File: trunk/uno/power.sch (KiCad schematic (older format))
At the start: 18 parts, among them Q1 FDN340P, U1 NCP1117 5V, U2 LP2985-33DBVR, U5 LM358

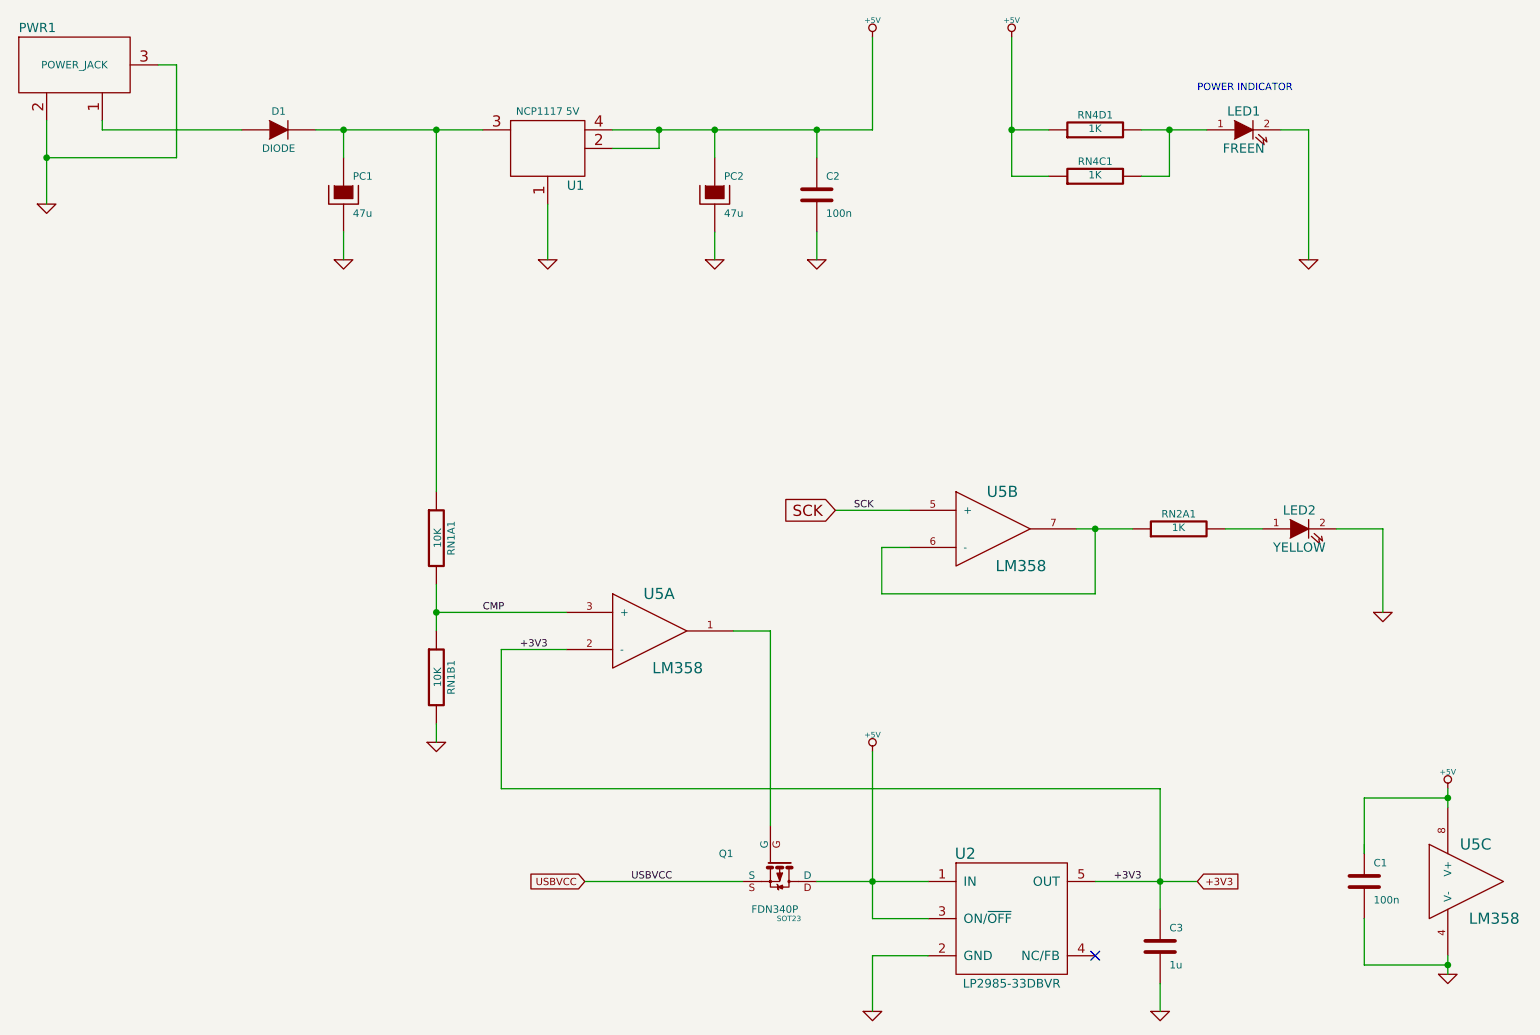
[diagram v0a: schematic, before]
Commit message: Schematic ERC passes. Circuit _might_ be complete, without errors. You just never know. :-P
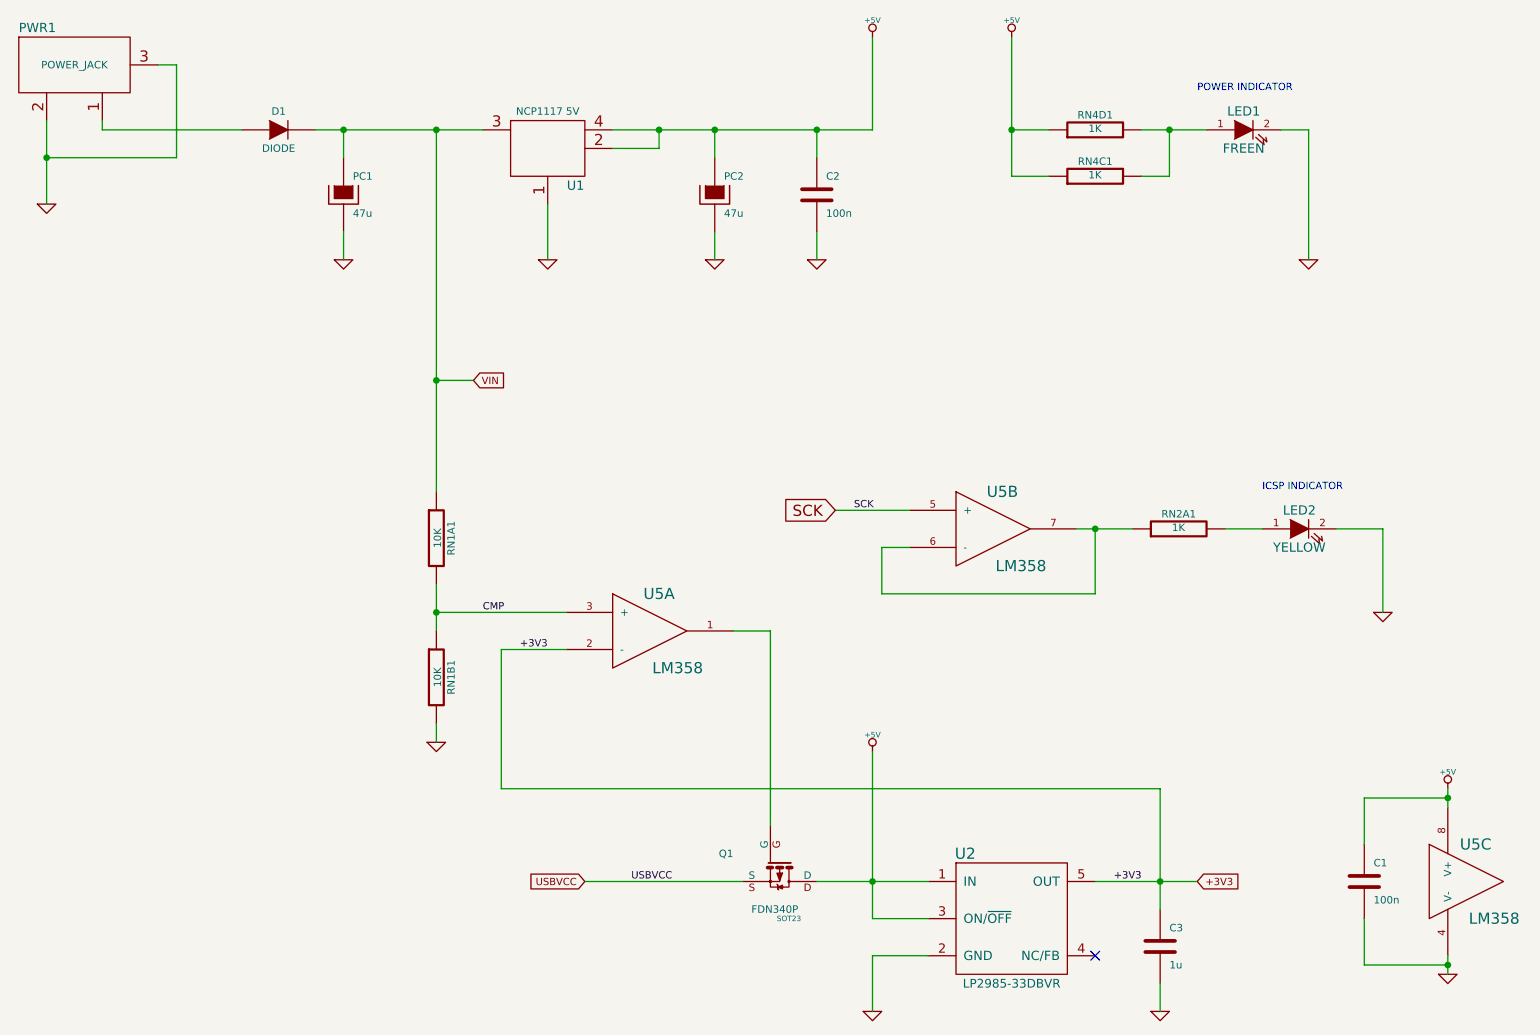
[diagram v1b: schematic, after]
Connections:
- net +5V: now also C1.1
- net VIN: now reaches D1.2 (K), PC1.1, RN1A1.1, U1.3 (IN)
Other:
- note added: "ICSP INDICATOR"
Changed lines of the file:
@@
 $EndComp
-Wire Wire Line
-	9200 5700 9200 5400
 Wire Wire Line
 	9200 5400 9650 5400
@@
 Text Notes 8300 1600 0    39   ~ 0
 POWER INDICATOR
+Text Notes 8650 3750 0    39   ~ 0
+ICSP INDICATOR
+Wire Wire Line
+	9200 5650 9200 5400
+Wire Wire Line
+	4200 3150 4400 3150
+Connection ~ 4200 3150
+Text GLabel 4400 3150 2    39   Input ~ 0
+VIN
 $EndSCHEMATC

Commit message: Component packages configured.
PCB initial placement.

Some minor typo corrections.
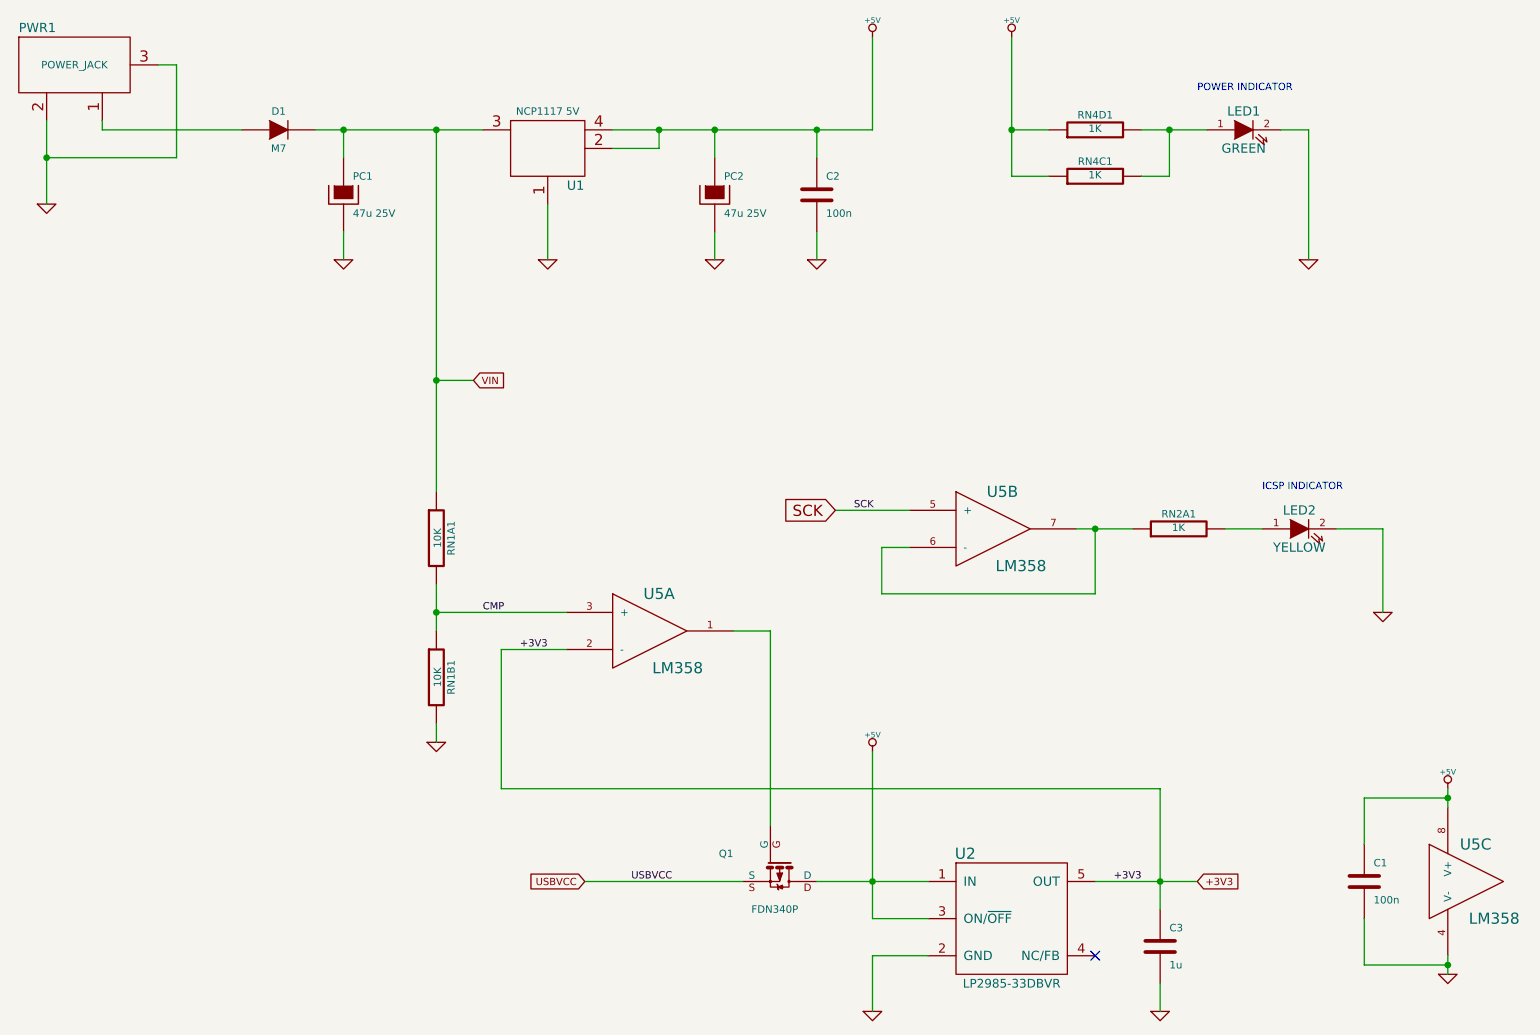
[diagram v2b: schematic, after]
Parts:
- C1, C2, C3: footprint ~ -> SM0603_Capa
- D1: value DIODE -> M7; footprint ~ -> DO-214AC
- LED1: value FREEN -> GREEN; footprint ~ -> LED_0603_GREEN
- LED2, RN1A1, RN1B1, RN2A1, RN4C1, RN4D1: footprint ~ -> (none)
- PC1, PC2: value 47u -> 47u 25V; footprint ~ -> (none)
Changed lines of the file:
@@
 Sheet 3 3
 Title "KiCADuino UNO Rev3"
-Date "24 jul 2013"
+Date "25 jul 2013"
 Rev "0.1"
 Comp "Gruvin & Co"
@@
 F 0 "U5" H 7250 4150 60  0000 C CNN
 F 1 "LM358" H 7350 3750 60  0000 C CNN
-F 2 "" H 7200 3950 60  0000 C CNN
+F 2 "" H 7200 3950 60  0001 C CNN
 F 3 "" H 7200 3950 60  0000 C CNN
 	2    7200 3950
@@
 F 0 "U5" H 5400 4700 60  0000 C CNN
 F 1 "LM358" H 5500 4300 60  0000 C CNN
-F 2 "" H 5350 4500 60  0000 C CNN
+F 2 "" H 5350 4500 60  0001 C CNN
 F 3 "" H 5350 4500 60  0000 C CNN
 	1    5350 4500
@@
 F 0 "U5" H 9800 6050 60  0000 C CNN
 F 1 "LM358" H 9900 5650 60  0000 C CNN
-F 2 "" H 9750 5850 60  0000 C CNN
+F 2 "" H 9750 5850 60  0001 C CNN
 F 3 "" H 9750 5850 60  0000 C CNN
 	3    9750 5850
@@
 F 0 "C1" H 9250 5950 40  0000 L CNN
 F 1 "100n" H 9250 5750 40  0000 L CNN
-F 2 "~" H 9238 5700 30  0000 C CNN
+F 2 "SM0603_Capa" H 9238 5700 30  0001 C CNN
 F 3 "~" H 9200 5850 60  0000 C CNN
 	1    9200 5850
@@
 F 0 "RN1A1" V 4280 4000 40  0000 C CNN
 F 1 "10K" V 4207 4001 40  0000 C CNN
-F 2 "~" V 4130 4000 30  0000 C CNN
+F 2 "" V 4130 4000 30  0001 C CNN
 F 3 "~" H 4200 4000 30  0000 C CNN
 	1    4200 4000
@@
 F 0 "RN1B1" V 4280 4750 40  0000 C CNN
 F 1 "10K" V 4207 4751 40  0000 C CNN
-F 2 "~" V 4130 4750 30  0000 C CNN
+F 2 "" V 4130 4750 30  0001 C CNN
 F 3 "~" H 4200 4750 30  0000 C CNN
 	1    4200 4750
@@
 F 0 "Q1" V 6000 5500 40  0000 R CNN
 F 1 "FDN340P" V 6300 5850 40  0000 R CNN
-F 2 "SOT23" V 6350 5800 29  0000 C CNN
+F 2 "SOT23" V 6350 5800 29  0001 C CNN
 F 3 "~" H 6050 5750 60  0000 C CNN
 	1    6050 5750
@@
 F 0 "RN2A1" V 8280 3950 40  0000 C CNN
 F 1 "1K" V 8207 3951 40  0000 C CNN
-F 2 "~" V 8130 3950 30  0000 C CNN
+F 2 "" V 8130 3950 30  0001 C CNN
 F 3 "~" H 8200 3950 30  0000 C CNN
 	1    8200 3950
@@
 F 0 "LED2" H 8850 4050 50  0000 C CNN
 F 1 "YELLOW" H 8850 3850 50  0000 C CNN
-F 2 "~" H 8850 3950 60  0000 C CNN
+F 2 "" H 8850 3950 60  0001 C CNN
 F 3 "~" H 8850 3950 60  0000 C CNN
 	1    8850 3950
@@
 F 0 "U2" H 7050 6400 60  0000 C CNN
 F 1 "LP2985-33DBVR" H 7300 5700 47  0000 C CNN
-F 2 "" H 7300 6050 60  0000 C CNN
+F 2 "" H 7300 6050 60  0001 C CNN
 F 3 "" H 7300 6050 60  0000 C CNN
 	1    7300 6050
@@
 F 0 "C3" H 8150 6300 40  0000 L CNN
 F 1 "1u" H 8150 6100 40  0000 L CNN
-F 2 "~" H 8138 6050 30  0000 C CNN
+F 2 "SM0603_Capa" H 8138 6050 30  0001 C CNN
 F 3 "~" H 8100 6200 60  0000 C CNN
 	1    8100 6200
@@
 F 0 "PWR1" H 2050 1650 50  0000 C CNN
 F 1 "POWER_JACK" H 2250 1450 40  0000 C CNN
-F 2 "" H 2250 1450 60  0000 C CNN
+F 2 "" H 2250 1450 60  0001 C CNN
 F 3 "" H 2250 1450 60  0000 C CNN
 	1    2250 1450
@@
 P 3350 1800
 F 0 "D1" H 3350 1900 40  0000 C CNN
-F 1 "DIODE" H 3350 1700 40  0000 C CNN
-F 2 "~" H 3350 1800 60  0000 C CNN
+F 1 "M7" H 3350 1700 40  0000 C CNN
+F 2 "DO-214AC" H 3350 1600 39  0001 C CNN
 F 3 "~" H 3350 1800 60  0000 C CNN
 	1    3350 1800
@@
 P 3700 2150
 F 0 "PC1" H 3750 2250 40  0000 L CNN
-F 1 "47u" H 3750 2050 40  0000 L CNN
-F 2 "~" H 3800 2000 30  0000 C CNN
+F 1 "47u 25V" H 3750 2050 40  0000 L CNN
+F 2 "" H 3800 2000 30  0001 C CNN
 F 3 "~" H 3700 2150 300 0000 C CNN
 	1    3700 2150
@@
 F 0 "U1" H 4950 1700 50  0000 C CNN
 F 1 "NCP1117 5V" H 4800 2100 40  0000 C CNN
-F 2 "" H 4800 1900 60  0000 C CNN
+F 2 "" H 4800 1900 60  0001 C CNN
 F 3 "" H 4800 1900 60  0000 C CNN
 	1    4800 1900
@@
 P 5700 2150
 F 0 "PC2" H 5750 2250 40  0000 L CNN
-F 1 "47u" H 5750 2050 40  0000 L CNN
-F 2 "~" H 5800 2000 30  0000 C CNN
+F 1 "47u 25V" H 5750 2050 40  0000 L CNN
+F 2 "" H 5800 2000 30  0001 C CNN
 F 3 "~" H 5700 2150 300 0000 C CNN
 	1    5700 2150
@@
 F 0 "C2" H 6300 2250 40  0000 L CNN
 F 1 "100n" H 6300 2050 40  0000 L CNN
-F 2 "~" H 6288 2000 30  0000 C CNN
+F 2 "SM0603_Capa" H 6288 2000 30  0001 C CNN
 F 3 "~" H 6250 2150 60  0000 C CNN
 	1    6250 2150
@@
 P 8550 1800
 F 0 "LED1" H 8550 1900 50  0000 C CNN
-F 1 "FREEN" H 8550 1700 50  0000 C CNN
-F 2 "~" H 8550 1800 60  0000 C CNN
+F 1 "GREEN" H 8550 1700 50  0000 C CNN
+F 2 "LED_0603_GREEN" H 8550 1800 60  0001 C CNN
 F 3 "~" H 8550 1800 60  0000 C CNN
 	1    8550 1800
@@
 F 0 "RN4D1" V 7830 1800 40  0000 C CNN
 F 1 "1K" V 7757 1801 40  0000 C CNN
-F 2 "~" V 7680 1800 30  0000 C CNN
+F 2 "" V 7680 1800 30  0001 C CNN
 F 3 "~" H 7750 1800 30  0000 C CNN
 	1    7750 1800
@@
 F 0 "RN4C1" V 7830 2050 40  0000 C CNN
 F 1 "1K" V 7757 2051 40  0000 C CNN
-F 2 "~" V 7680 2050 30  0000 C CNN
+F 2 "" V 7680 2050 30  0001 C CNN
 F 3 "~" H 7750 2050 30  0000 C CNN
 	1    7750 2050

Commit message: Added resistor network part/module for RN1-4 (no 3D package yet).
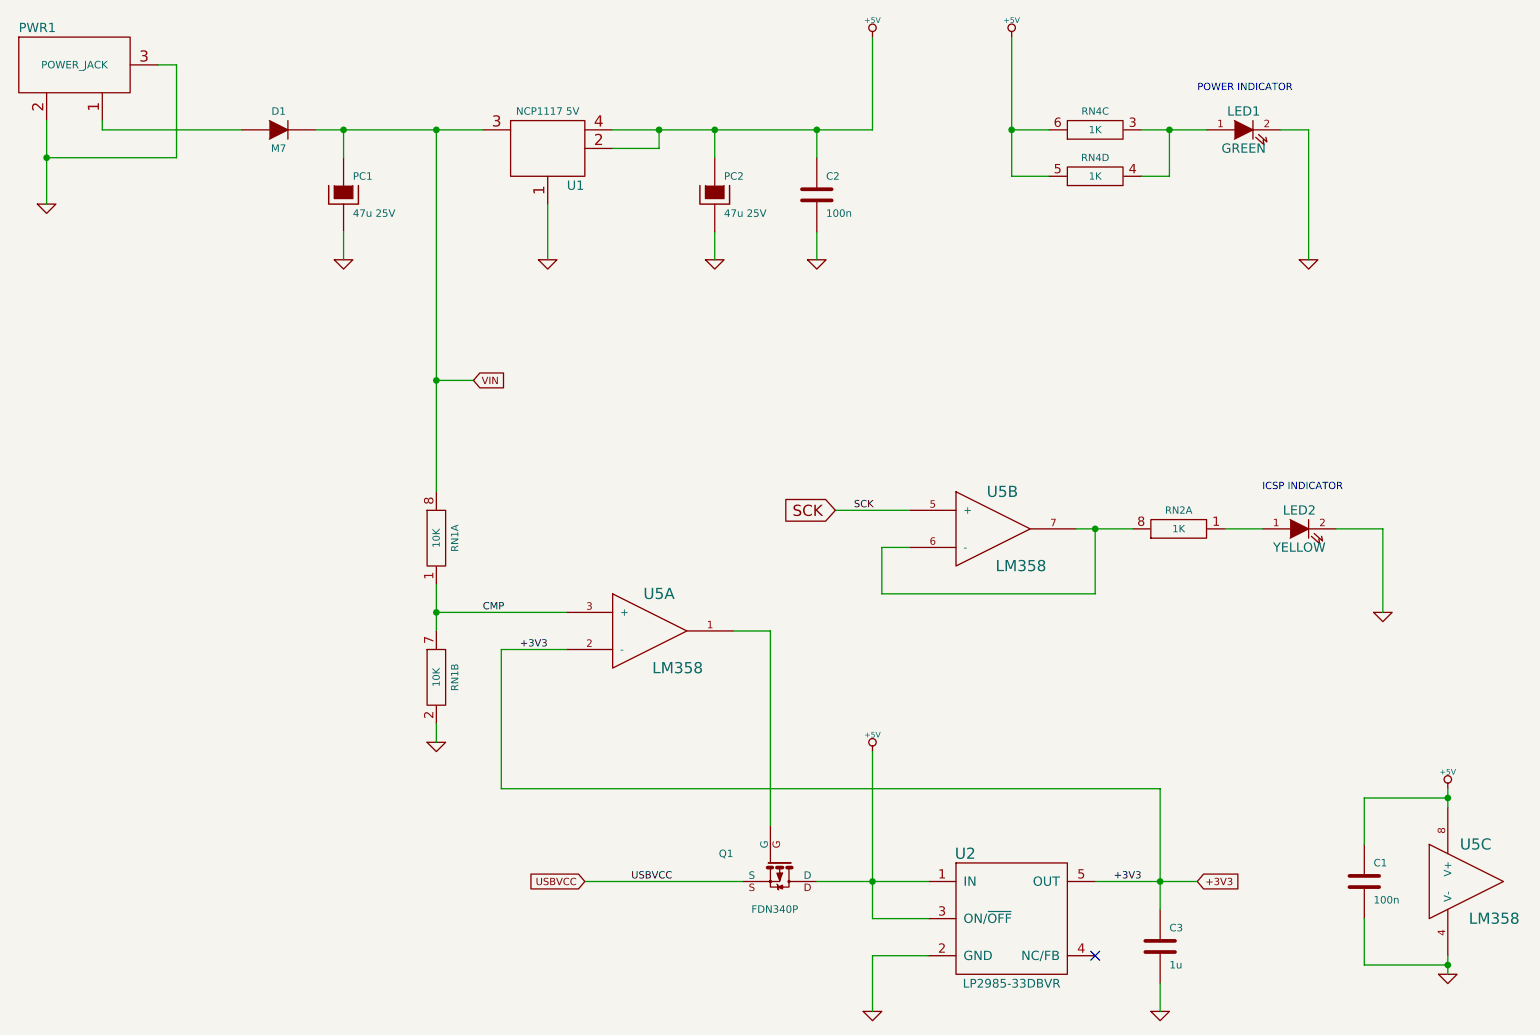
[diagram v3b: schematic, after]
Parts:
- removed RN1A1, RN1B1: 10K, symbol R
- removed RN2A1, RN4C1, RN4D1: 1K, symbol R
- added RN1: 10K, symbol R_NET4
- added RN2, RN4: 1K, symbol R_NET4
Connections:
- net +5V: now also RN4.5 (6), RN4.6
- net CMP: now also RN1.1 (3), RN1.7 (6)
- net GND: now also RN1.2 (3)
- net VIN: now also RN1.8 (6)
- net at U5.6 (-), U5.7: now also RN2.8 (6)
- net at LED2.1 (A): now also RN2.1 (3)
- net at LED1.1 (A): now also RN4.3, RN4.4 (3)
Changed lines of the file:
@@
 	9200 6300 9650 6300
 Connection ~ 9650 6300
-$Comp
-L R RN1A1
-U 1 1 51EFCCC0
-P 4200 4000
-F 0 "RN1A1" V 4280 4000 40  0000 C CNN
-F 1 "10K" V 4207 4001 40  0000 C CNN
-F 2 "" V 4130 4000 30  0001 C CNN
-F 3 "~" H 4200 4000 30  0000 C CNN
-	1    4200 4000
-	1    0    0    -1
-$EndComp
-$Comp
-L R RN1B1
-U 1 1 51EFCCCD
-P 4200 4750
-F 0 "RN1B1" V 4280 4750 40  0000 C CNN
-F 1 "10K" V 4207 4751 40  0000 C CNN
-F 2 "" V 4130 4750 30  0001 C CNN
-F 3 "~" H 4200 4750 30  0000 C CNN
-	1    4200 4750
-	1    0    0    -1
-$EndComp
 Wire Wire Line
 	4900 4400 4200 4400
@@
 	7650 3950 7950 3950
 $Comp
-L R RN2A1
-U 1 1 51EFD8AC
-P 8200 3950
-F 0 "RN2A1" V 8280 3950 40  0000 C CNN
-F 1 "1K" V 8207 3951 40  0000 C CNN
-F 2 "" V 8130 3950 30  0001 C CNN
-F 3 "~" H 8200 3950 30  0000 C CNN
-	1    8200 3950
-	0    -1   -1   0
-$EndComp
-$Comp
 L LED LED2
 U 1 1 51EFD8B4
@@
 	1    0    0    -1
 $EndComp
-$Comp
-L R RN4D1
-U 1 1 51EFF2F2
-P 7750 1800
-F 0 "RN4D1" V 7830 1800 40  0000 C CNN
-F 1 "1K" V 7757 1801 40  0000 C CNN
-F 2 "" V 7680 1800 30  0001 C CNN
-F 3 "~" H 7750 1800 30  0000 C CNN
-	1    7750 1800
-	0    -1   -1   0
-$EndComp
-$Comp
-L R RN4C1
-U 1 1 51EFF2F8
-P 7750 2050
-F 0 "RN4C1" V 7830 2050 40  0000 C CNN
-F 1 "1K" V 7757 2051 40  0000 C CNN
-F 2 "" V 7680 2050 30  0001 C CNN
-F 3 "~" H 7750 2050 30  0000 C CNN
-	1    7750 2050
-	0    -1   -1   0
-$EndComp
 Wire Wire Line
 	8000 1800 8350 1800
@@
 Text GLabel 4400 3150 2    39   Input ~ 0
 VIN
+$Comp
+L R_NET4 RN1
+U 1 1 51F113F4
+P 4200 4000
+F 0 "RN1" V 4300 4000 39  0000 C CNN
+F 1 "10K" V 4200 4000 39  0000 C CNN
+F 2 "" H 4200 4000 60  0000 C CNN
+F 3 "" H 4200 4000 60  0000 C CNN
+	1    4200 4000
+	1    0    0    -1
+$EndComp
+$Comp
+L R_NET4 RN1
+U 2 1 51F1141E
+P 4200 4750
+F 0 "RN1" V 4300 4750 39  0000 C CNN
+F 1 "10K" V 4200 4750 39  0000 C CNN
+F 2 "" H 4200 4750 60  0000 C CNN
+F 3 "" H 4200 4750 60  0000 C CNN
+	2    4200 4750
+	1    0    0    -1
+$EndComp
+$Comp
+L R_NET4 RN2
+U 1 1 51F11A9C
+P 8200 3950
+F 0 "RN2" V 8300 3950 39  0000 C CNN
+F 1 "1K" V 8200 3950 39  0000 C CNN
+F 2 "" H 8200 3950 60  0000 C CNN
+F 3 "" H 8200 3950 60  0000 C CNN
+	1    8200 3950
+	0    -1   -1   0
+$EndComp
+$Comp
+L R_NET4 RN4
+U 3 1 51F11F83
+P 7750 1800
+F 0 "RN4" V 7850 1800 39  0000 C CNN
+F 1 "1K" V 7750 1800 39  0000 C CNN
+F 2 "" H 7750 1800 60  0000 C CNN
+F 3 "" H 7750 1800 60  0000 C CNN
+	3    7750 1800
+	0    -1   -1   0
+$EndComp
+$Comp
+L R_NET4 RN4
+U 4 1 51F11F95
+P 7750 2050
+F 0 "RN4" V 7850 2050 39  0000 C CNN
+F 1 "1K" V 7750 2050 39  0000 C CNN
+F 2 "" H 7750 2050 60  0000 C CNN
+F 3 "" H 7750 2050 60  0000 C CNN
+	4    7750 2050
+	0    -1   -1   0
+$EndComp
 $EndSCHEMATC
